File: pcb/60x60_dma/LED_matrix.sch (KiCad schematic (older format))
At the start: 5 parts, among them U3 74HC595, U4 TBD62783A, U5 TLC5916

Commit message: - add some testpoints
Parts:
- U5: symbol ti:TLC5916 -> bcl4v2-rescue:TLC5916-ti
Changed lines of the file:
@@
 $EndComp
 $Comp
-L ti:TLC5916 U5
+L bcl4v2-rescue:TLC5916-ti U5
 U 1 1 5C401A25
 P 7650 4050
+AR Path="/5C401A25" Ref="U5"  Part="1"
+AR Path="/5BD6AFE7/5C401A25" Ref="U5"  Part="1"
 F 0 "U5" H 7400 4550 50  0000 C CNN
 F 1 "TLC5916" H 7900 4550 50  0000 C CNN

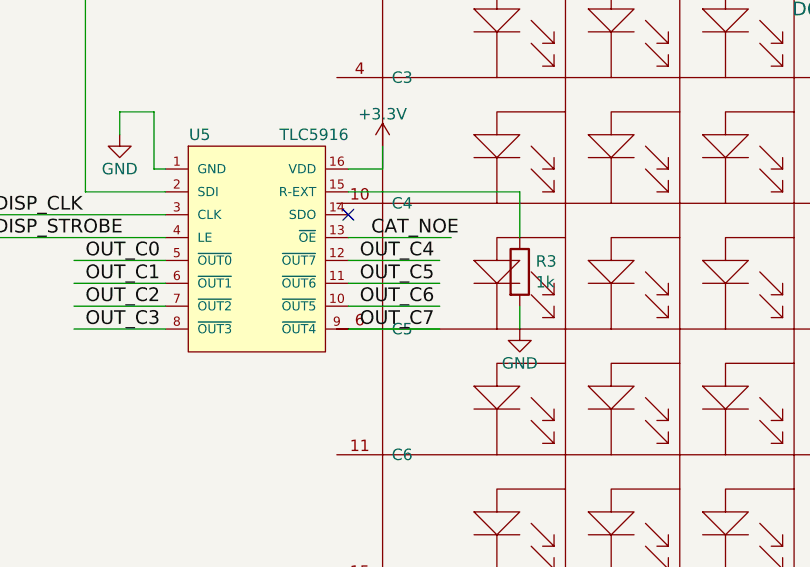
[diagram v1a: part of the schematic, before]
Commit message: - fix display connections, add testpoints
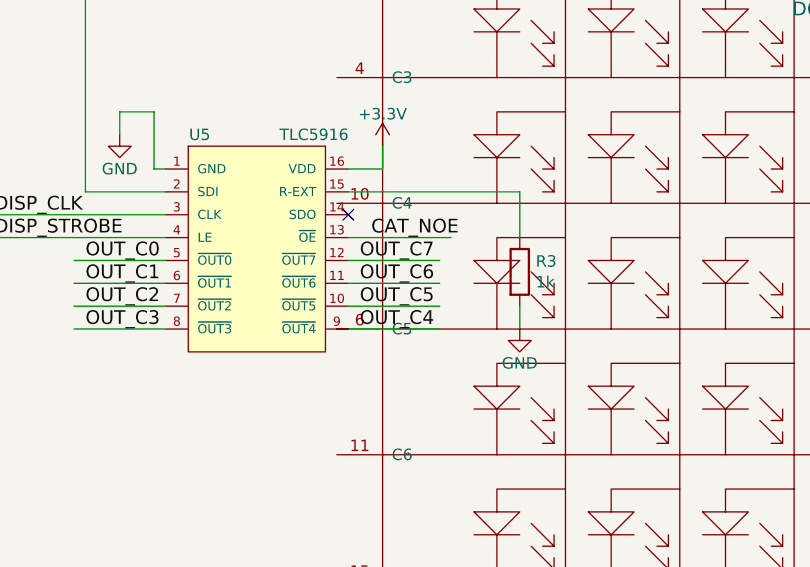
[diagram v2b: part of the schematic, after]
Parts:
- U4: footprint Housings_SOIC:SOIC-18W_7.5x11.6mm_Pitch1.27mm -> kicad_lib:badger_SOIC-18W_7.5x11.6mm_Pitch1.27mm
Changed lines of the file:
@@
 Text Label 6900 4400 0    60   ~ 0
 OUT_C3
+Text Label 8100 4400 0    60   ~ 0
+OUT_C4
+Text Label 8100 4300 0    60   ~ 0
+OUT_C5
+Text Label 8100 4200 0    60   ~ 0
+OUT_C6
 Text Label 8100 4100 0    60   ~ 0
-OUT_C4
-Text Label 8100 4200 0    60   ~ 0
-OUT_C5
-Text Label 8100 4300 0    60   ~ 0
-OUT_C6
-Text Label 8100 4400 0    60   ~ 0
 OUT_C7
 Text Label 6900 4100 0    60   ~ 0
@@
 F 0 "U4" H 7300 2500 50  0000 C CNN
 F 1 "TBD62783A" H 7800 2500 50  0000 C CNN
-F 2 "Housings_SOIC:SOIC-18W_7.5x11.6mm_Pitch1.27mm" H 7550 1500 50  0001 C CNN
+F 2 "kicad_lib:badger_SOIC-18W_7.5x11.6mm_Pitch1.27mm" H 7550 1500 50  0001 C CNN
 F 3 "http://toshiba.semicon-storage.com/info/docget.jsp?did=30523&prodName=TBD62783APG" H 7250 2450 50  0001 C CNN
 	1    7550 2050

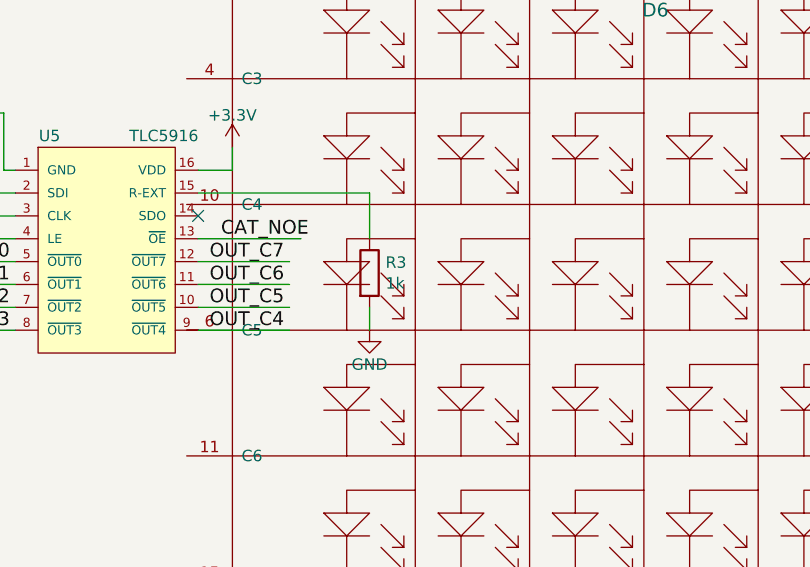
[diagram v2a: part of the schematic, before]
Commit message: - add OSHV logo, move LED a bit
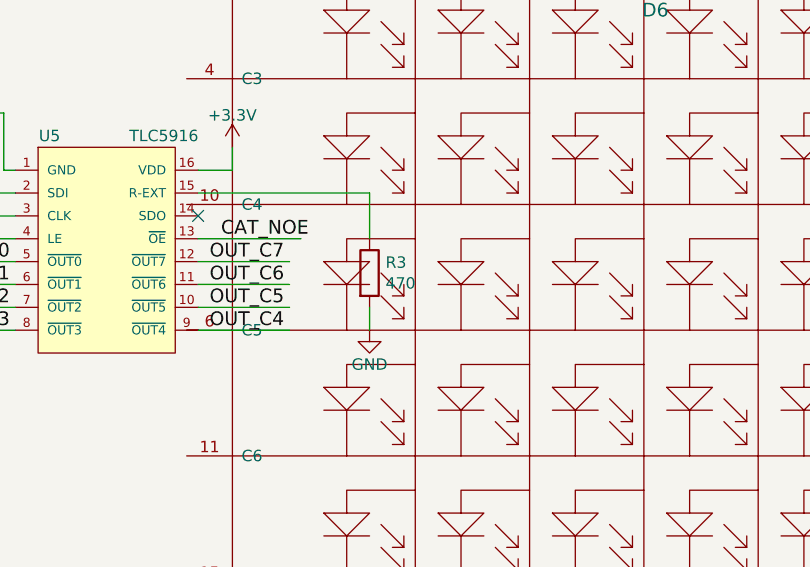
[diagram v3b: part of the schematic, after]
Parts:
- R3: value 1k -> 470
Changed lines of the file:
@@
 P 8800 4150
 F 0 "R3" H 8870 4196 50  0000 L CNN
-F 1 "1k" H 8870 4105 50  0000 L CNN
+F 1 "470" H 8870 4105 50  0000 L CNN
 F 2 "Resistors_SMD:R_0805_HandSoldering" V 8730 4150 50  0001 C CNN
 F 3 "" H 8800 4150 50  0001 C CNN

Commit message: - clense the schematics
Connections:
- wire segments 70 -> 75
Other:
- moved on the sheet: D6, R3, U3, U4, U5
